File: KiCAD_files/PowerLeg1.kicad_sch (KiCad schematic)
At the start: 63 parts, among them Q301 IPD200N15N3, Q302 IPD200N15N3, Q303 IPD200N15N3, U301 AMC1100DUB, U302 ACS730xLCTR-20AB, U303 UCC21222DR, U304 OPA316, U305 OPA316, U306 SFH617A-2X009T

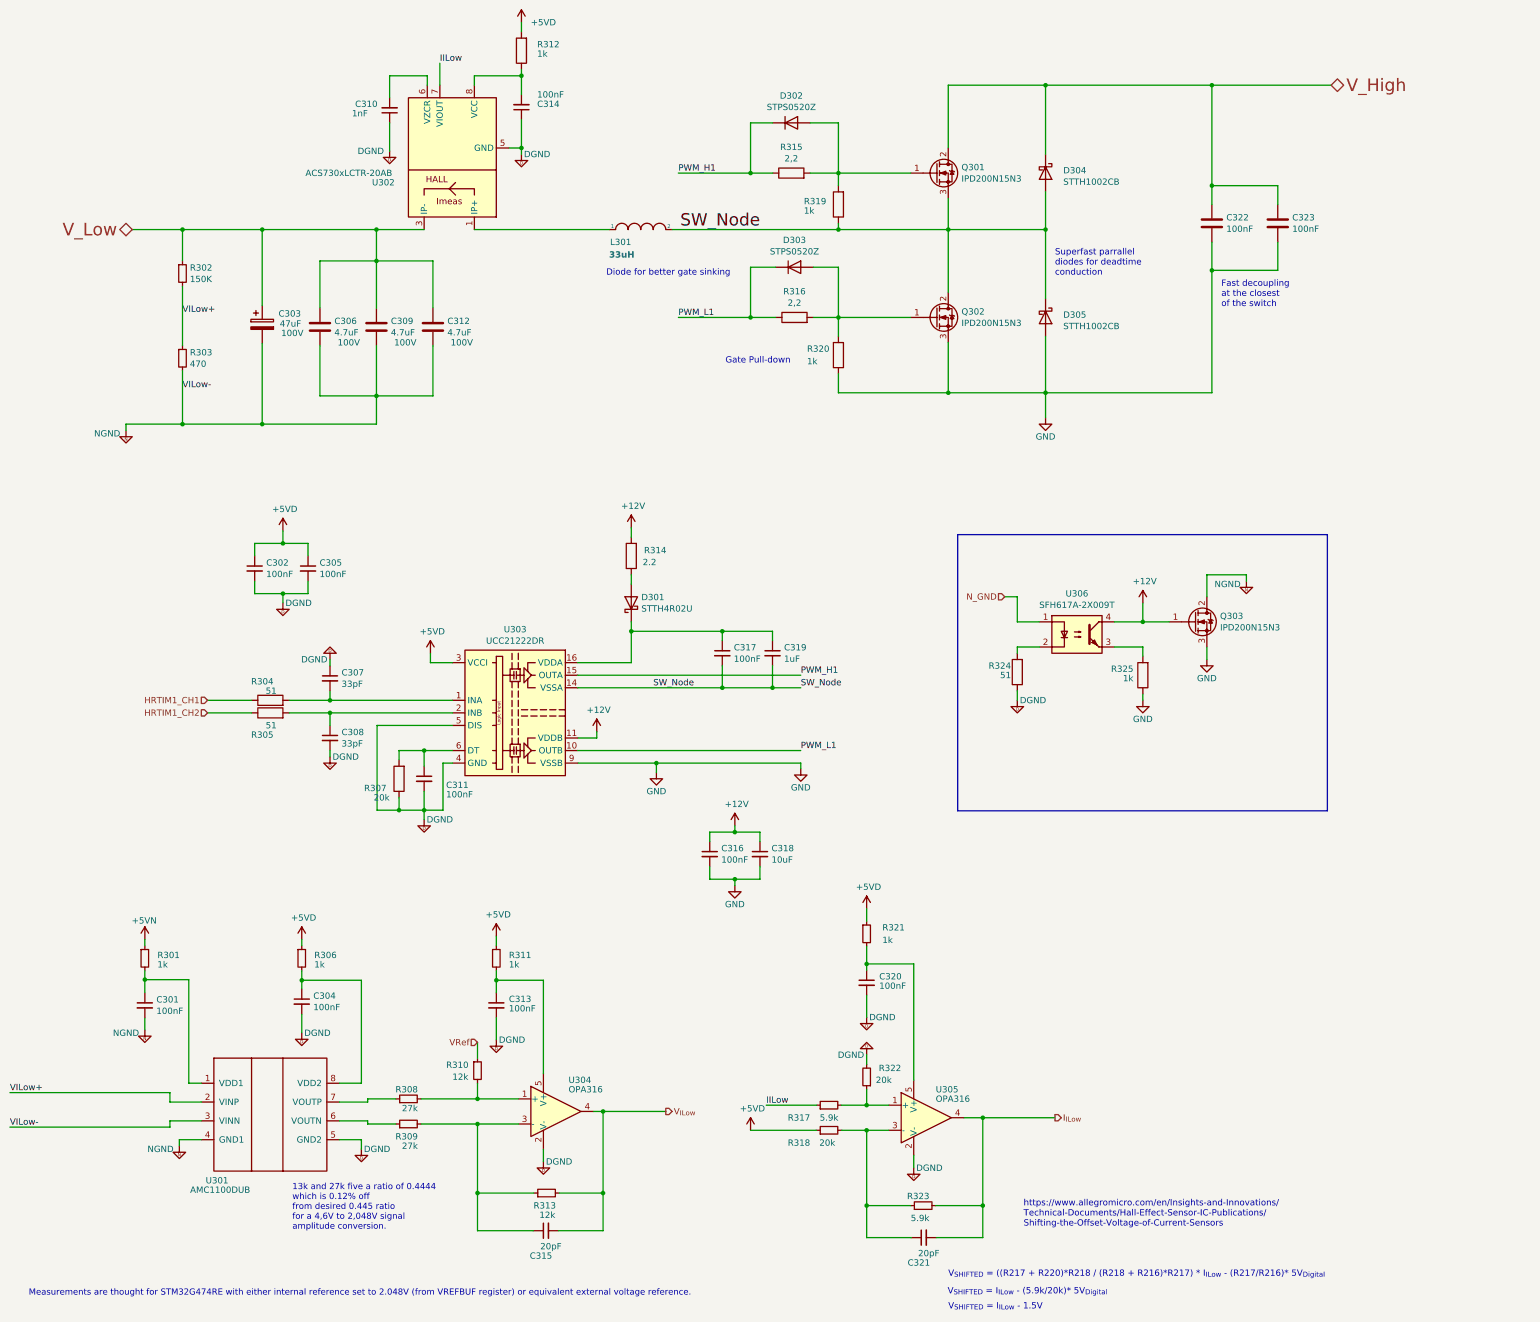
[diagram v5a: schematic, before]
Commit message: WIP : Routed last sensors to the MCU, tweaked the courtiyards ERC almost passing
Former-commit-id: ade1cde8d39341e78235fc8e83a4a1c667a0d829
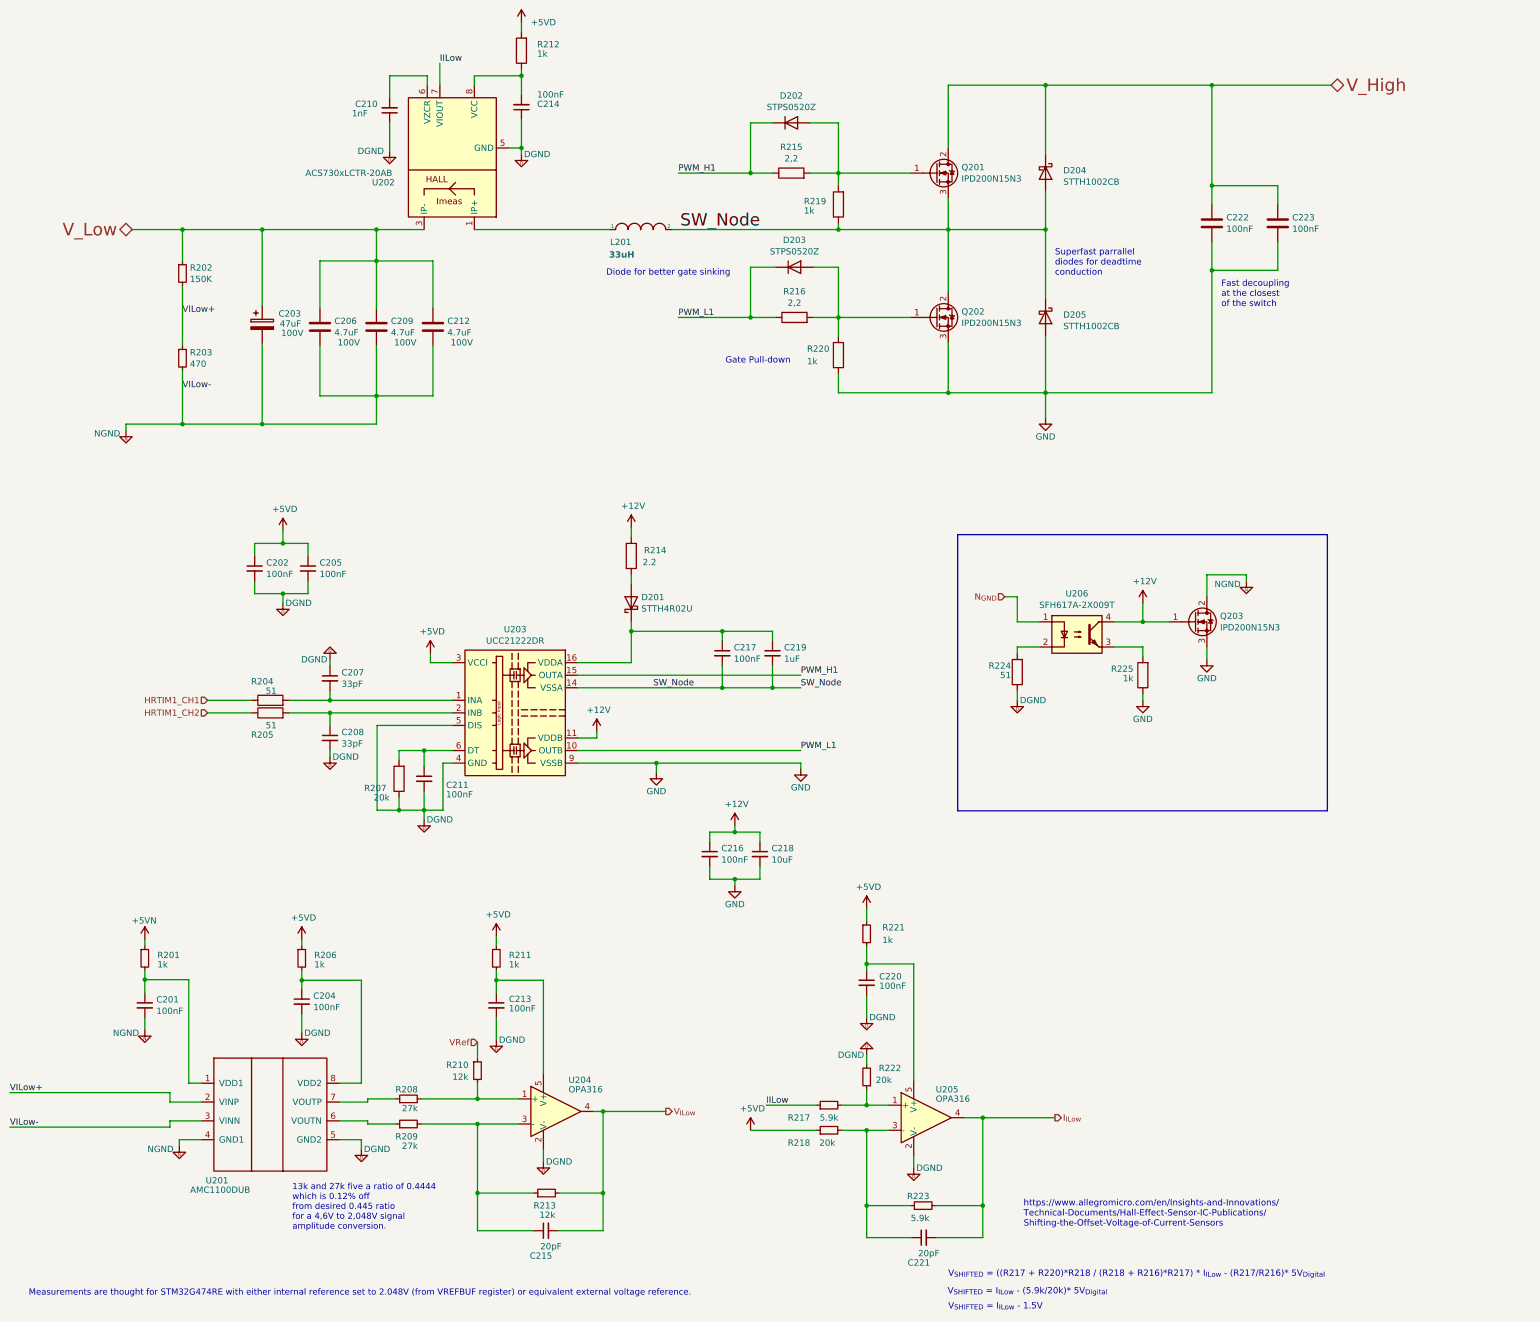
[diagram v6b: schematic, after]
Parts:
- C202: renamed from C302; footprint Capacitor_SMD:C_0805_2012Metric -> Footprints:C_0805_2012Metric
- C205: renamed from C305; footprint Capacitor_SMD:C_0805_2012Metric -> Footprints:C_0805_2012Metric
- C206: renamed from C306; footprint Capacitor_SMD:C_1210_3225Metric -> Footprints:C_1210_3225Metric
- C207: renamed from C307; footprint Capacitor_SMD:C_0805_2012Metric -> Footprints:C_0805_2012Metric
- C208: renamed from C308; footprint Capacitor_SMD:C_0805_2012Metric -> Footprints:C_0805_2012Metric
- C209: renamed from C309; footprint Capacitor_SMD:C_1210_3225Metric -> Footprints:C_1210_3225Metric
- C210: renamed from C310; footprint Capacitor_SMD:C_0805_2012Metric -> Footprints:C_0805_2012Metric
- C211: renamed from C311; footprint Capacitor_SMD:C_0805_2012Metric -> Footprints:C_0805_2012Metric
- C212: renamed from C312; footprint Capacitor_SMD:C_1210_3225Metric -> Footprints:C_1210_3225Metric
- C213: renamed from C313; footprint Capacitor_SMD:C_0805_2012Metric -> Footprints:C_0805_2012Metric
- C215: renamed from C315; footprint Capacitor_SMD:C_0805_2012Metric -> Footprints:C_0805_2012Metric
- C216: renamed from C316; footprint Capacitor_SMD:C_0805_2012Metric -> Footprints:C_0805_2012Metric
- C217: renamed from C317; footprint Capacitor_SMD:C_0805_2012Metric -> Footprints:C_0805_2012Metric
- C218: renamed from C318; footprint Capacitor_SMD:C_1210_3225Metric -> Footprints:C_1210_3225Metric
- C219: renamed from C319; footprint Capacitor_SMD:C_0805_2012Metric -> Footprints:C_0805_2012Metric
- C220: renamed from C320; footprint Capacitor_SMD:C_0805_2012Metric -> Footprints:C_0805_2012Metric
- C221: renamed from C321; footprint Capacitor_SMD:C_0805_2012Metric -> Footprints:C_0805_2012Metric
- C222: renamed from C322; footprint Capacitor_SMD:C_0805_2012Metric -> Footprints:C_0805_2012Metric
- C223: renamed from C323; footprint Capacitor_SMD:C_1210_3225Metric -> Footprints:C_1210_3225Metric
- D202: renamed from D302; footprint Diode_SMD:D_SOD-323 -> Footprints:D_SOD-323
- D203: renamed from D303; footprint Diode_SMD:D_SOD-323 -> Footprints:D_SOD-323
- R201: renamed from R301; footprint Resistor_SMD:R_0805_2012Metric -> Footprints:R_0805_2012Metric
- R202: renamed from R302; footprint Resistor_SMD:R_0805_2012Metric -> Footprints:R_0805_2012Metric
- R203: renamed from R303; footprint Resistor_SMD:R_0805_2012Metric -> Footprints:R_0805_2012Metric
- R204: renamed from R304; footprint Resistor_SMD:R_0805_2012Metric -> Footprints:R_0805_2012Metric
- R205: renamed from R305; footprint Resistor_SMD:R_0805_2012Metric -> Footprints:R_0805_2012Metric
- R206: renamed from R306; footprint Resistor_SMD:R_0805_2012Metric -> Footprints:R_0805_2012Metric
- R207: renamed from R307; footprint Resistor_SMD:R_0805_2012Metric -> Footprints:R_0805_2012Metric
- R208: renamed from R308; footprint Resistor_SMD:R_0805_2012Metric -> Footprints:R_0805_2012Metric
- R209: renamed from R309; footprint Resistor_SMD:R_0805_2012Metric -> Footprints:R_0805_2012Metric
- R210: renamed from R310; footprint Resistor_SMD:R_0805_2012Metric -> Footprints:R_0805_2012Metric
- R211: renamed from R311; footprint Resistor_SMD:R_0805_2012Metric -> Footprints:R_0805_2012Metric
- R212: renamed from R312; footprint Resistor_SMD:R_0805_2012Metric -> Footprints:R_0805_2012Metric
- R213: renamed from R313; footprint Resistor_SMD:R_0805_2012Metric -> Footprints:R_0805_2012Metric
- R214: renamed from R314; footprint Resistor_SMD:R_0805_2012Metric -> Footprints:R_0805_2012Metric
- R215: renamed from R315; footprint Resistor_SMD:R_0805_2012Metric -> Footprints:R_0805_2012Metric
- R216: renamed from R316; footprint Resistor_SMD:R_0805_2012Metric -> Footprints:R_0805_2012Metric
- R217: renamed from R317; footprint Resistor_SMD:R_0805_2012Metric -> Footprints:R_0805_2012Metric
- R218: renamed from R318; footprint Resistor_SMD:R_0805_2012Metric -> Footprints:R_0805_2012Metric
- R219: renamed from R319; footprint Resistor_SMD:R_0805_2012Metric -> Footprints:R_0805_2012Metric
- R220: renamed from R320; footprint Resistor_SMD:R_0805_2012Metric -> Footprints:R_0805_2012Metric
- R221: renamed from R321; footprint Resistor_SMD:R_0805_2012Metric -> Footprints:R_0805_2012Metric
- R222: renamed from R322; footprint Resistor_SMD:R_0805_2012Metric -> Footprints:R_0805_2012Metric
- R223: renamed from R323; footprint Resistor_SMD:R_0805_2012Metric -> Footprints:R_0805_2012Metric
- R224: renamed from R324; footprint Resistor_SMD:R_0805_2012Metric -> Footprints:R_0805_2012Metric
- R225: renamed from R325; footprint Resistor_SMD:R_0805_2012Metric -> Footprints:R_0805_2012Metric
- renumbered C301 to C201, C303 to C203, C304 to C204, C314 to C214, D301 to D201, D304 to D204, D305 to D205, L301 to L201, Q301 to Q201, Q302 to Q202, Q303 to Q203, U301 to U201, U302 to U202, U303 to U203, U304 to U204, U305 to U205, U306 to U206
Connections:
- net N_GND renamed N_{GND}

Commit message: WIP : Started correcting MCU board mistakes
Former-commit-id: 0e34b6d72e10d1eac13c8cf31fc8e8f14d7f468b
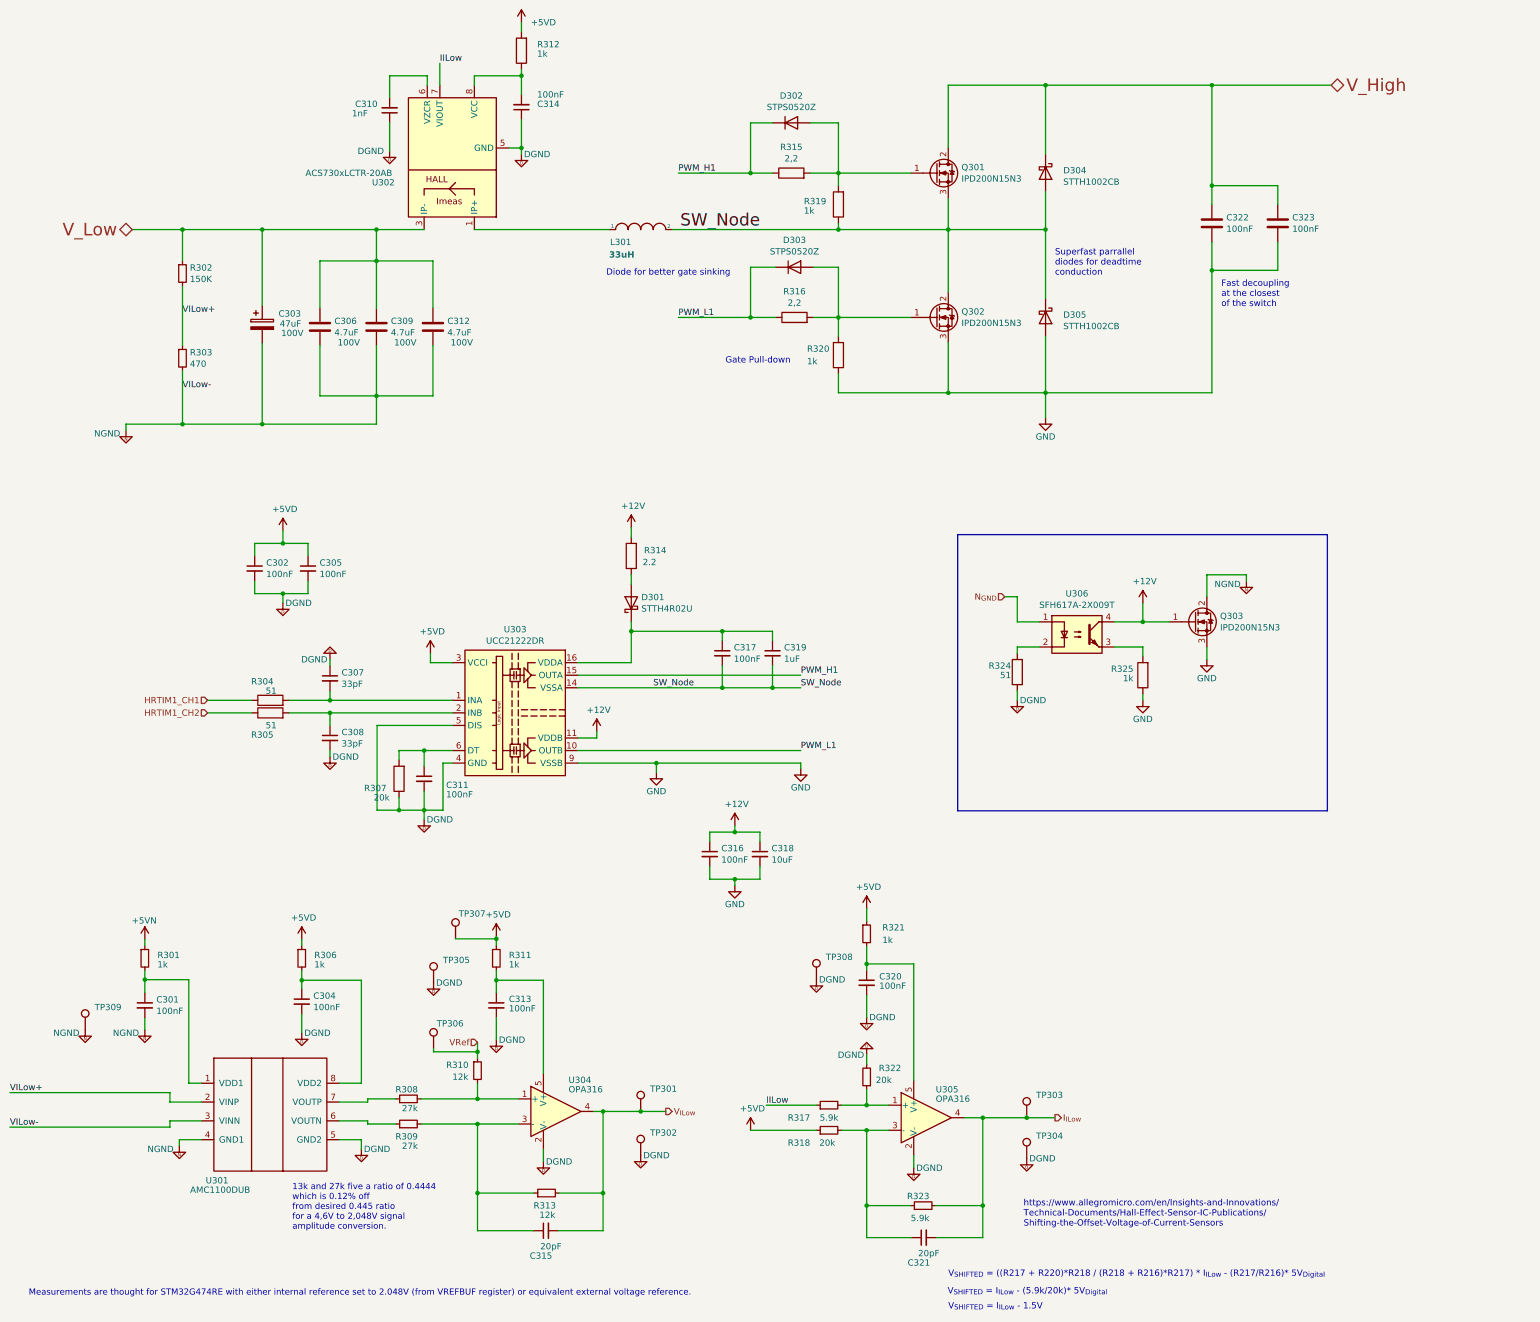
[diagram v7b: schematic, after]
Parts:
- added TP301, TP302, TP303, TP304, TP305, TP306, TP307, TP308, TP309: TestPoint, TestPoint:TestPoint_Pad_D1.0mm, symbol Connector:TestPoint
- renumbered C201 to C301, C202 to C302, C203 to C303, C204 to C304, C205 to C305, C206 to C306, C207 to C307, C208 to C308, C209 to C309, C210 to C310, C211 to C311, C212 to C312, C213 to C313, C214 to C314, C215 to C315, C216 to C316, C217 to C317, C218 to C318, C219 to C319, C220 to C320, C221 to C321, C222 to C322, C223 to C323, D201 to D301, D202 to D302, D203 to D303, D204 to D304, D205 to D305, L201 to L301, Q201 to Q301, Q202 to Q302, Q203 to Q303, R201 to R301, R202 to R302, R203 to R303, R204 to R304, R205 to R305, R206 to R306, R207 to R307, R208 to R308, R209 to R309, R210 to R310, R211 to R311, R212 to R312, R213 to R313, R214 to R314, R215 to R315, R216 to R316, R217 to R317, R218 to R318, R219 to R319, R220 to R320, R221 to R321, R222 to R322, R223 to R323, R224 to R324, R225 to R325, U201 to U301, U202 to U302, U203 to U303, U204 to U304, U205 to U305, U206 to U306
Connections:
- net +5VD: now also TP307.1
- net DGND: now also TP302.1, TP304.1, TP305.1, TP308.1
- net I_{ILow}: now also TP303.1
- net NGND: now also TP309.1
- net VRef: now also TP306.1
- net V_{ILow}: now also TP301.1
